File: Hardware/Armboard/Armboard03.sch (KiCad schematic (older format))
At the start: 8 parts

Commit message: H-Bridge completed
Completed the H-Bridge Hierarchal Sheet
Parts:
- U? (x8): symbol MRDT_Shields:TM4C129E_Launchpad -> Armboard-rescue:TM4C129E_Launchpad-MRDT_Shields
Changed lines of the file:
@@
 $EndDescr
 $Comp
-L MRDT_Shields:TM4C129E_Launchpad U?
+L Armboard-rescue:TM4C129E_Launchpad-MRDT_Shields U?
 U 1 1 5F752485
 P 3810 3400
@@
 $EndComp
 $Comp
-L MRDT_Shields:TM4C129E_Launchpad U?
+L Armboard-rescue:TM4C129E_Launchpad-MRDT_Shields U?
 U 2 1 5F752EEB
 P 4310 3400
@@
 $EndComp
 $Comp
-L MRDT_Shields:TM4C129E_Launchpad U?
+L Armboard-rescue:TM4C129E_Launchpad-MRDT_Shields U?
 U 3 1 5F753E3C
 P 3800 5520
@@
 $EndComp
 $Comp
-L MRDT_Shields:TM4C129E_Launchpad U?
+L Armboard-rescue:TM4C129E_Launchpad-MRDT_Shields U?
 U 4 1 5F754D60
 P 4300 5520
@@
 $EndComp
 $Comp
-L MRDT_Shields:TM4C129E_Launchpad U?
+L Armboard-rescue:TM4C129E_Launchpad-MRDT_Shields U?
 U 5 1 5F755C93
 P 6400 3390
@@
 $EndComp
 $Comp
-L MRDT_Shields:TM4C129E_Launchpad U?
+L Armboard-rescue:TM4C129E_Launchpad-MRDT_Shields U?
 U 6 1 5F7570A2
 P 6900 3390
@@
 $EndComp
 $Comp
-L MRDT_Shields:TM4C129E_Launchpad U?
+L Armboard-rescue:TM4C129E_Launchpad-MRDT_Shields U?
 U 7 1 5F757FE4
 P 6420 5520
@@
 $EndComp
 $Comp
-L MRDT_Shields:TM4C129E_Launchpad U?
+L Armboard-rescue:TM4C129E_Launchpad-MRDT_Shields U?
 U 8 1 5F7598C0
 P 6920 5520

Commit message: Added serial pins, limit switches, titles, and indicators
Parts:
- U? (x8): symbol Armboard-rescue:TM4C129E_Launchpad-MRDT_Shields -> Armboard-rescue:TM4C129E_Launchpad-MRDT_Shields-Armboard-rescue
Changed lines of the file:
@@
 $EndDescr
 $Comp
-L Armboard-rescue:TM4C129E_Launchpad-MRDT_Shields U?
+L Armboard-rescue:TM4C129E_Launchpad-MRDT_Shields-Armboard-rescue U?
 U 1 1 5F752485
 P 3810 3400
@@
 $EndComp
 $Comp
-L Armboard-rescue:TM4C129E_Launchpad-MRDT_Shields U?
+L Armboard-rescue:TM4C129E_Launchpad-MRDT_Shields-Armboard-rescue U?
 U 2 1 5F752EEB
 P 4310 3400
@@
 $EndComp
 $Comp
-L Armboard-rescue:TM4C129E_Launchpad-MRDT_Shields U?
+L Armboard-rescue:TM4C129E_Launchpad-MRDT_Shields-Armboard-rescue U?
 U 3 1 5F753E3C
 P 3800 5520
@@
 $EndComp
 $Comp
-L Armboard-rescue:TM4C129E_Launchpad-MRDT_Shields U?
+L Armboard-rescue:TM4C129E_Launchpad-MRDT_Shields-Armboard-rescue U?
 U 4 1 5F754D60
 P 4300 5520
@@
 $EndComp
 $Comp
-L Armboard-rescue:TM4C129E_Launchpad-MRDT_Shields U?
+L Armboard-rescue:TM4C129E_Launchpad-MRDT_Shields-Armboard-rescue U?
 U 5 1 5F755C93
 P 6400 3390
@@
 $EndComp
 $Comp
-L Armboard-rescue:TM4C129E_Launchpad-MRDT_Shields U?
+L Armboard-rescue:TM4C129E_Launchpad-MRDT_Shields-Armboard-rescue U?
 U 6 1 5F7570A2
 P 6900 3390
@@
 $EndComp
 $Comp
-L Armboard-rescue:TM4C129E_Launchpad-MRDT_Shields U?
+L Armboard-rescue:TM4C129E_Launchpad-MRDT_Shields-Armboard-rescue U?
 U 7 1 5F757FE4
 P 6420 5520
@@
 $EndComp
 $Comp
-L Armboard-rescue:TM4C129E_Launchpad-MRDT_Shields U?
+L Armboard-rescue:TM4C129E_Launchpad-MRDT_Shields-Armboard-rescue U?
 U 8 1 5F7598C0
 P 6920 5520

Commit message: Tiva Updates
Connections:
- net +3V3: now reaches U?.+3V3 (A1_1)
- net +3V3: now also U?.+3V3' (A2_1)
- net LS_3: now reaches U?.PB2 (A1_9)
- net LS_4: now reaches U?.PB3 (A1_10)
- net Rx_1_Tiva: now reaches U?.PC4 (A1_3)
- net Tx_1_Tiva: now reaches U?.PC5 (A1_4)
- net GND: now reaches U?.GND (B1_2)
- net GND: now also U?.GND (B2_2), U?.GND (D1_1), U?.GND (D2_1)
- net Enc_1_PWM: now reaches U?.PF1 (C1_1)
- net Enc_2_PWM: now reaches U?.PF2 (C1_2)
- net Enc_3_PWM: now reaches U?.PF3 (C1_3)
- net Enc_4_PWM: now reaches U?.PG0 (C1_4)
- net Rx_3_Tiva: now reaches U?.PP0 (A2_3)
- net Tx_3_Tiva: now reaches U?.PP1 (A2_4)
- net LS_1: now reaches U?.PA4 (B2_9)
- net LS_2: now reaches U?.PA5 (B2_10)
- net Rx_2_Tiva: now reaches U?.PK0 (B2_5)
- net Tx_2_Tiva: now reaches U?.PK1 (B2_6)
- net Enc_5_PWM: now reaches U?.PG1 (C2_1)
- net Laser_Control: now reaches U?.PH0 (C2_7)
- net Solenoid_Actuation: now reaches U?.PH1 (C2_8)
- net Enc_6_PWM: now reaches U?.PK4 (C2_2)
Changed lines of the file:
@@
 	-1   0    0    -1
 $EndComp
+$Comp
+L power:GND #PWR?
+U 1 1 5F83BEC8
+P 4800 2600
+F 0 "#PWR?" H 4800 2350 50  0001 C CNN
+F 1 "GND" H 4805 2427 50  0000 C CNN
+F 2 "" H 4800 2600 50  0001 C CNN
+F 3 "" H 4800 2600 50  0001 C CNN
+	1    4800 2600
+	1    0    0    -1
+$EndComp
+Wire Wire Line
+	4500 2550 4510 2550
+Wire Wire Line
+	4800 2550 4800 2600
+Connection ~ 4510 2550
+Wire Wire Line
+	4510 2550 4800 2550
+$Comp
+L power:+3.3V #PWR?
+U 1 1 5F83D247
+P 3400 2450
+F 0 "#PWR?" H 3400 2300 50  0001 C CNN
+F 1 "+3.3V" V 3415 2578 50  0000 L CNN
+F 2 "" H 3400 2450 50  0001 C CNN
+F 3 "" H 3400 2450 50  0001 C CNN
+	1    3400 2450
+	0    -1   -1   0
+$EndComp
+Wire Wire Line
+	3400 2450 3610 2450
+$Comp
+L power:+3.3V #PWR?
+U 1 1 5F83FA68
+P 5990 2440
+F 0 "#PWR?" H 5990 2290 50  0001 C CNN
+F 1 "+3.3V" V 6005 2568 50  0000 L CNN
+F 2 "" H 5990 2440 50  0001 C CNN
+F 3 "" H 5990 2440 50  0001 C CNN
+	1    5990 2440
+	0    -1   -1   0
+$EndComp
+Wire Wire Line
+	5990 2440 6200 2440
+$Comp
+L power:GND #PWR?
+U 1 1 5F83FD93
+P 7390 2560
+F 0 "#PWR?" H 7390 2310 50  0001 C CNN
+F 1 "GND" H 7395 2387 50  0000 C CNN
+F 2 "" H 7390 2560 50  0001 C CNN
+F 3 "" H 7390 2560 50  0001 C CNN
+	1    7390 2560
+	1    0    0    -1
+$EndComp
+$Comp
+L power:GND #PWR?
+U 1 1 5F83FFBB
+P 4790 4620
+F 0 "#PWR?" H 4790 4370 50  0001 C CNN
+F 1 "GND" H 4795 4447 50  0000 C CNN
+F 2 "" H 4790 4620 50  0001 C CNN
+F 3 "" H 4790 4620 50  0001 C CNN
+	1    4790 4620
+	1    0    0    -1
+$EndComp
+Wire Wire Line
+	4790 4570 4790 4620
+Wire Wire Line
+	4500 4570 4790 4570
+$Comp
+L power:GND #PWR?
+U 1 1 5F8401EF
+P 7410 4620
+F 0 "#PWR?" H 7410 4370 50  0001 C CNN
+F 1 "GND" H 7415 4447 50  0000 C CNN
+F 2 "" H 7410 4620 50  0001 C CNN
+F 3 "" H 7410 4620 50  0001 C CNN
+	1    7410 4620
+	1    0    0    -1
+$EndComp
+Wire Wire Line
+	7410 4570 7410 4620
+Wire Wire Line
+	7120 4570 7410 4570
+Text GLabel 3530 4570 0    50   Input ~ 0
+Enc_1_PWM
+Wire Wire Line
+	3600 4570 3530 4570
+Text GLabel 3530 4670 0    50   Input ~ 0
+Enc_2_PWM
+Wire Wire Line
+	3600 4670 3530 4670
+Text GLabel 3530 4770 0    50   Input ~ 0
+Enc_3_PWM
+Wire Wire Line
+	3600 4770 3530 4770
+Text GLabel 3530 4870 0    50   Input ~ 0
+Enc_4_PWM
+Wire Wire Line
+	3600 4870 3530 4870
+Text GLabel 6150 4570 0    50   Input ~ 0
+Enc_5_PWM
+Wire Wire Line
+	6220 4570 6150 4570
+Text GLabel 6150 4670 0    50   Input ~ 0
+Enc_6_PWM
+Wire Wire Line
+	6220 4670 6150 4670
+Text GLabel 7170 3340 2    50   Input ~ 0
+LS_2
+Wire Wire Line
+	7100 3340 7170 3340
+Text GLabel 7170 3240 2    50   Input ~ 0
+LS_1
+Wire Wire Line
+	7100 3240 7170 3240
+Text GLabel 3540 3250 0    50   Input ~ 0
+LS_3
+Wire Wire Line
+	3610 3250 3540 3250
+Text GLabel 3540 3350 0    50   Input ~ 0
+LS_4
+Wire Wire Line
+	3610 3350 3540 3350
+Text GLabel 6150 5170 0    50   Input ~ 0
+Laser_Control
+Wire Wire Line
+	6220 5170 6150 5170
+Text GLabel 6150 5270 0    50   Input ~ 0
+Solenoid_Actuation
+Wire Wire Line
+	6220 5270 6150 5270
+Text GLabel 3540 2650 0    50   Input ~ 0
+Rx_1_Tiva
+Wire Wire Line
+	3610 2650 3540 2650
+Text GLabel 3540 2750 0    50   Input ~ 0
+Tx_1_Tiva
+Wire Wire Line
+	3610 2750 3540 2750
+Text GLabel 7170 2940 2    50   Input ~ 0
+Tx_2_Tiva
+Wire Wire Line
+	7100 2940 7170 2940
+Text GLabel 7170 2840 2    50   Input ~ 0
+Rx_2_Tiva
+Wire Wire Line
+	7100 2840 7170 2840
+Wire Wire Line
+	7100 2540 7390 2540
+Wire Wire Line
+	7390 2540 7390 2560
+Text GLabel 6130 2640 0    50   Input ~ 0
+Rx_3_Tiva
+Wire Wire Line
+	6200 2640 6130 2640
+Text GLabel 6130 2740 0    50   Input ~ 0
+Tx_3_Tiva
+Wire Wire Line
+	6200 2740 6130 2740
 $EndSCHEMATC

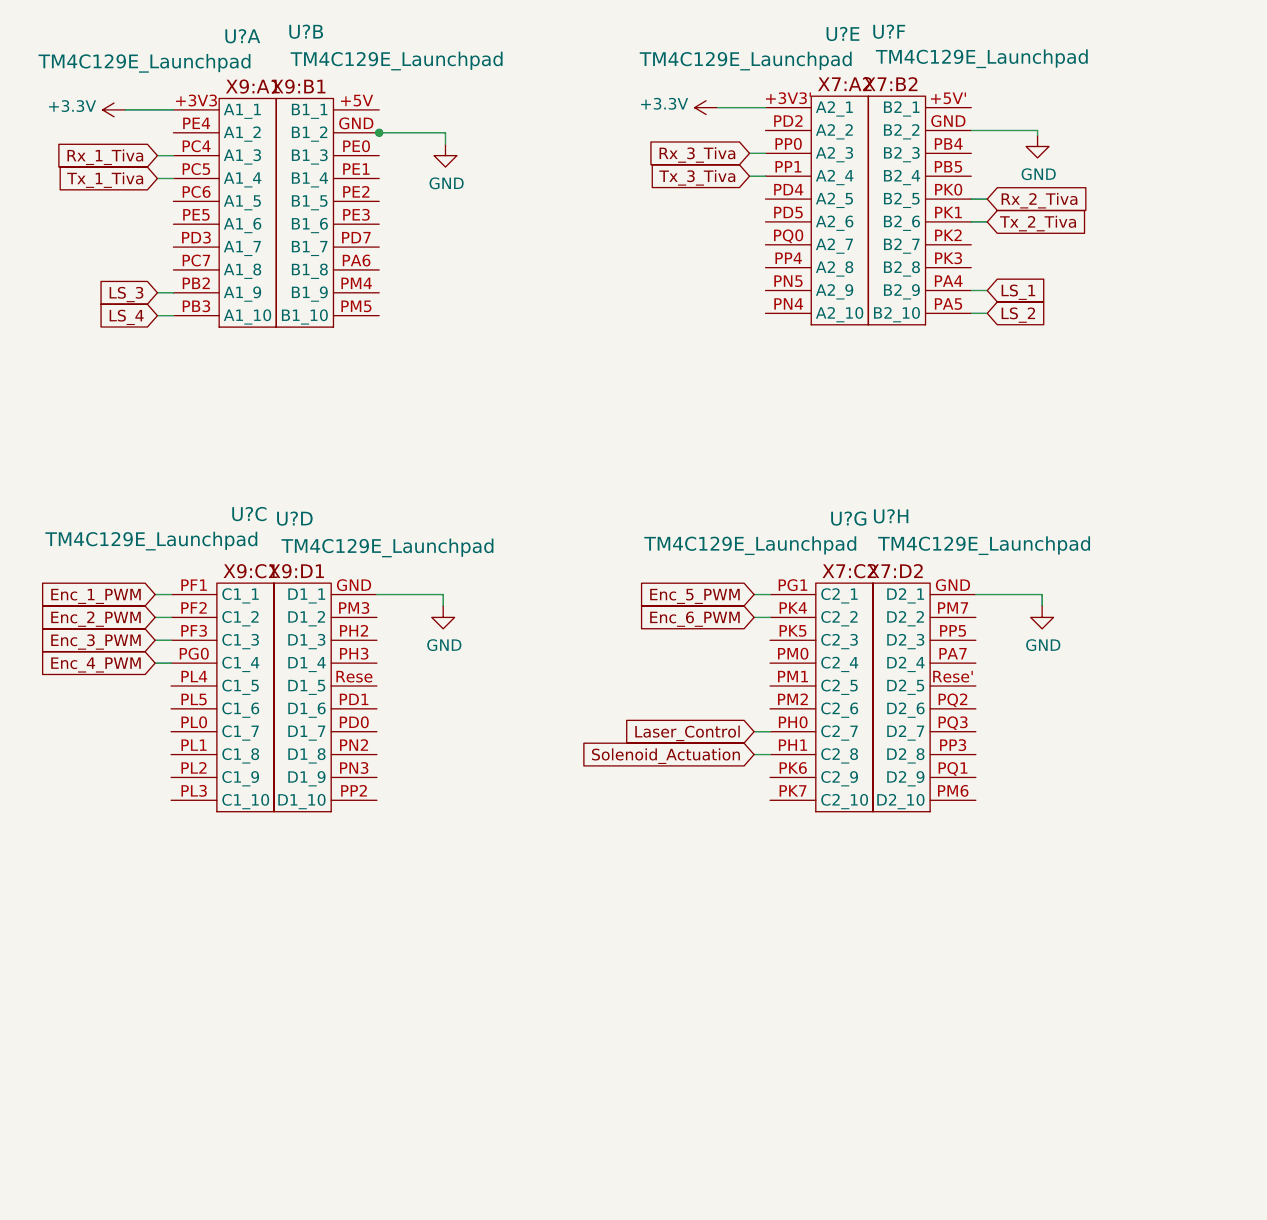
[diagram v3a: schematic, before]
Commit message: Formatted GNDs and added motor toggle buttons
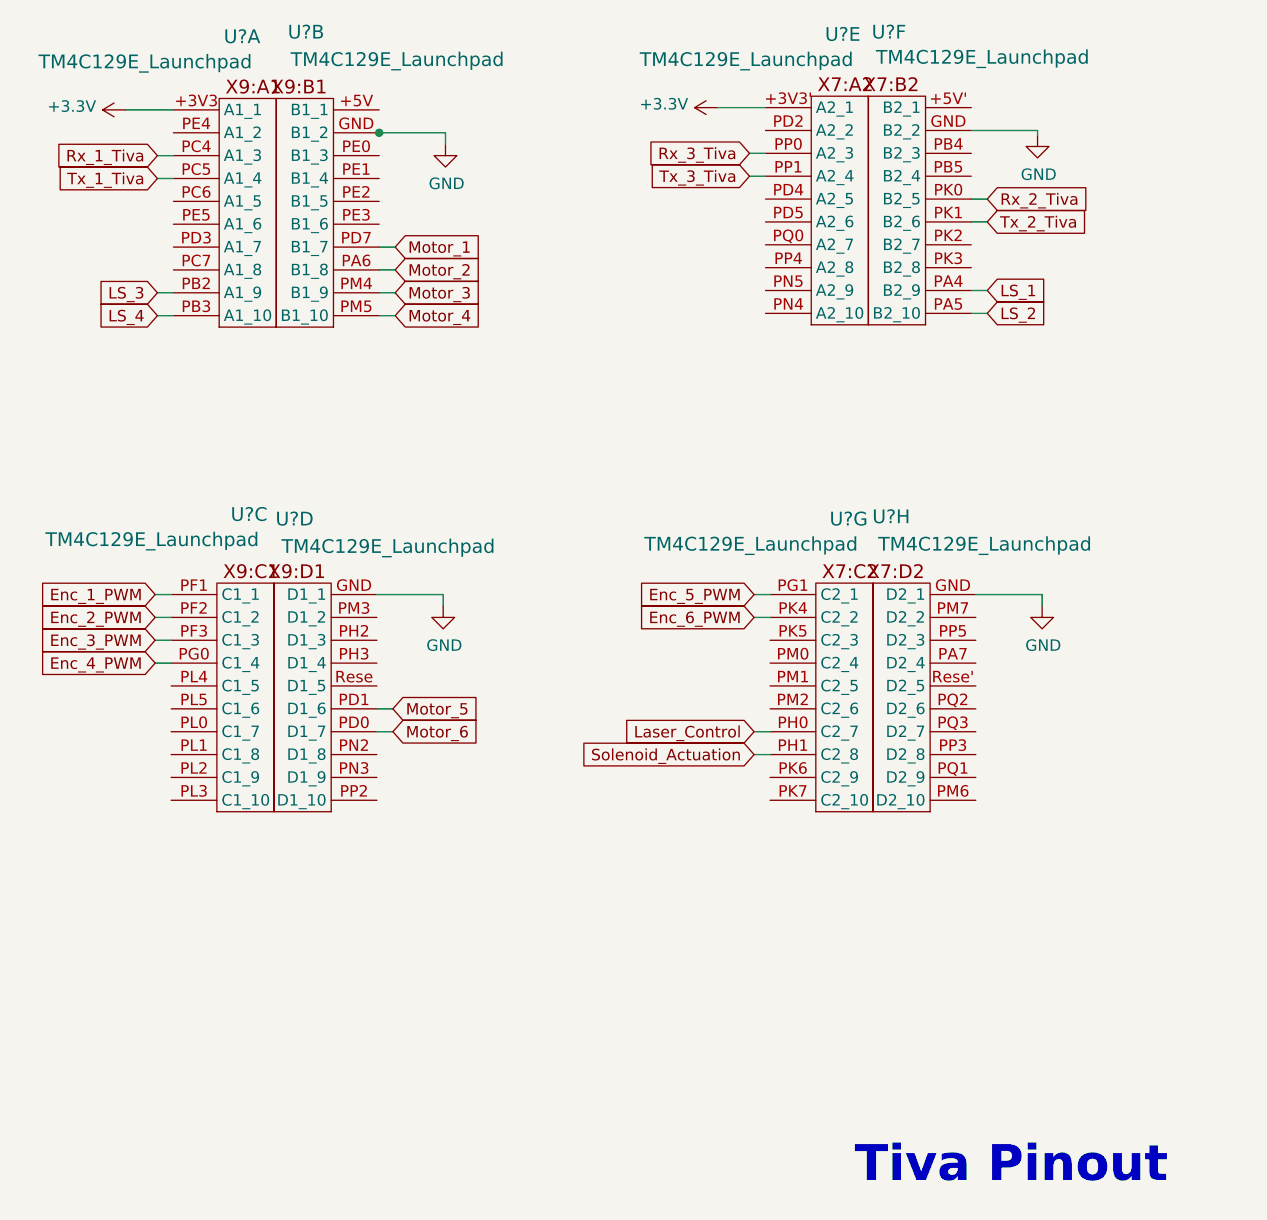
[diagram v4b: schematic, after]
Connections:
- net Motor_2: now reaches U?.PA6 (B1_8)
- net Motor_1: now reaches U?.PD7 (B1_7)
- net Motor_3: now reaches U?.PM4 (B1_9)
- net Motor_4: now reaches U?.PM5 (B1_10)
- net Motor_6: now reaches U?.PD0 (D1_7)
- net Motor_5: now reaches U?.PD1 (D1_6)
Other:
- note added: "Tiva Pinout"
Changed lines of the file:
@@
 Wire Wire Line
 	6200 2740 6130 2740
+Text GLabel 4580 3150 2    50   Input ~ 0
+Motor_2
+Wire Wire Line
+	4510 3150 4580 3150
+Text GLabel 4580 3050 2    50   Input ~ 0
+Motor_1
+Wire Wire Line
+	4510 3050 4580 3050
+Text GLabel 4580 3350 2    50   Input ~ 0
+Motor_4
+Wire Wire Line
+	4510 3350 4580 3350
+Text GLabel 4580 3250 2    50   Input ~ 0
+Motor_3
+Wire Wire Line
+	4510 3250 4580 3250
+Text GLabel 4570 5170 2    50   Input ~ 0
+Motor_6
+Wire Wire Line
+	4500 5170 4570 5170
+Text GLabel 4570 5070 2    50   Input ~ 0
+Motor_5
+Wire Wire Line
+	4500 5070 4570 5070
+Text Notes 6590 7160 0    157  ~ 31
+Tiva Pinout
 $EndSCHEMATC

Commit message: Fixed buttons/switches page, changed resistor values, fixed some tiva connections
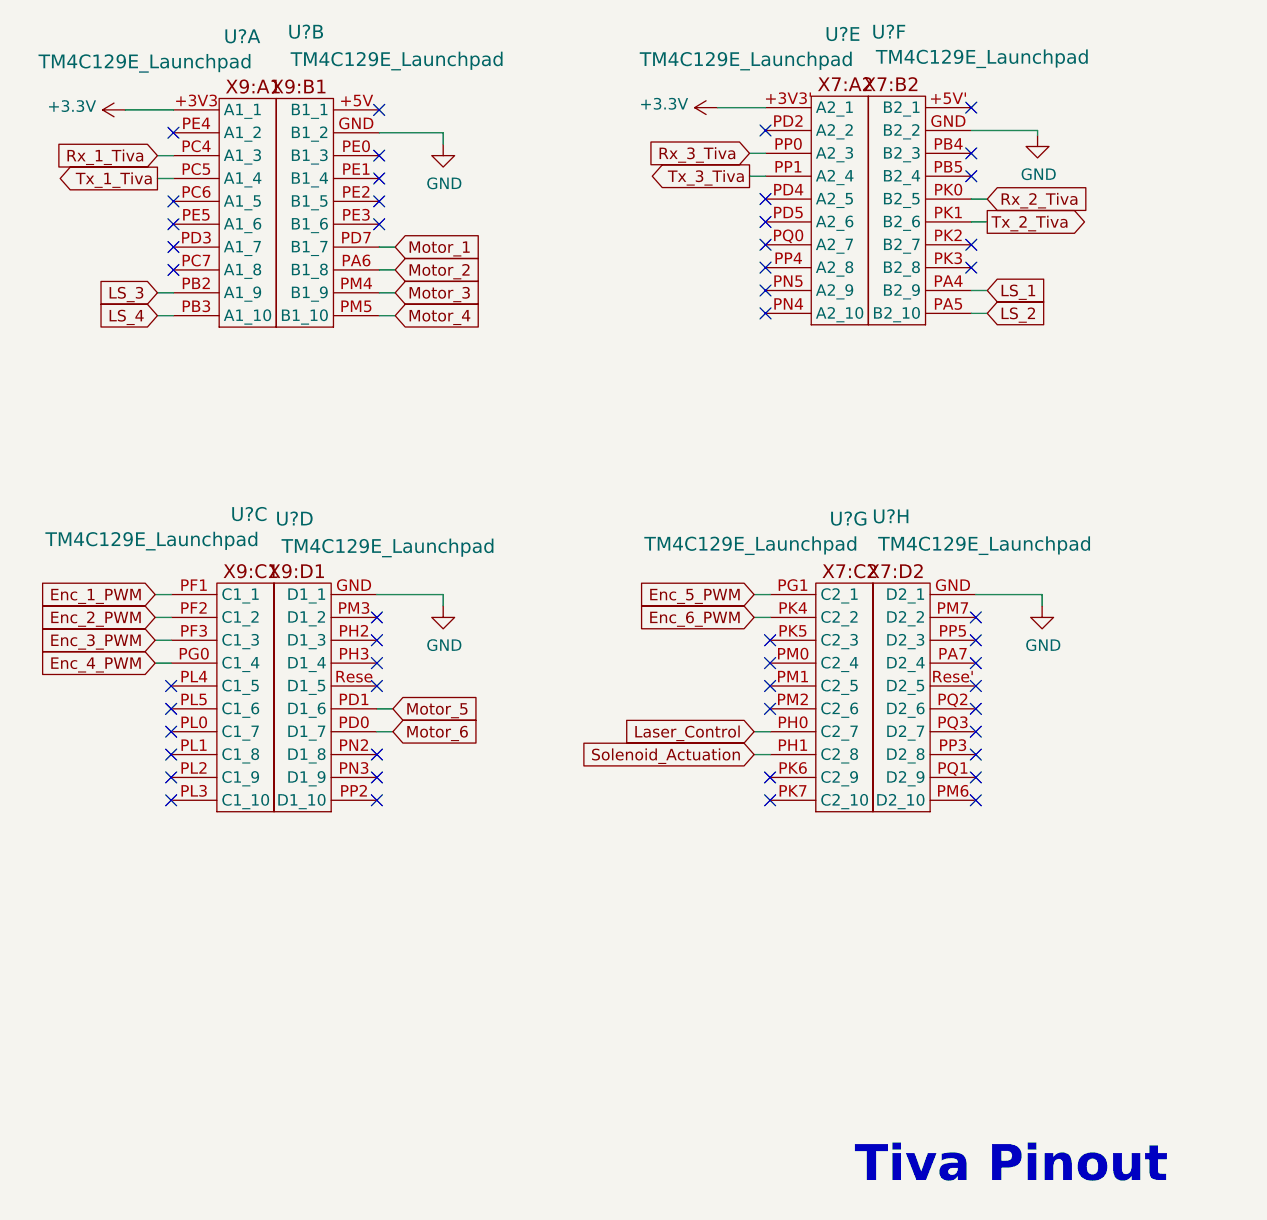
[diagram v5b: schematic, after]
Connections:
- no-connect marks 0 -> 50
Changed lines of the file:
@@
 L power:GND #PWR?
 U 1 1 5F83BEC8
-P 4800 2600
-F 0 "#PWR?" H 4800 2350 50  0001 C CNN
-F 1 "GND" H 4805 2427 50  0000 C CNN
-F 2 "" H 4800 2600 50  0001 C CNN
-F 3 "" H 4800 2600 50  0001 C CNN
-	1    4800 2600
-	1    0    0    -1
-$EndComp
-Wire Wire Line
-	4500 2550 4510 2550
-Wire Wire Line
-	4800 2550 4800 2600
-Connection ~ 4510 2550
-Wire Wire Line
-	4510 2550 4800 2550
+P 4790 2600
+F 0 "#PWR?" H 4790 2350 50  0001 C CNN
+F 1 "GND" H 4795 2427 50  0000 C CNN
+F 2 "" H 4790 2600 50  0001 C CNN
+F 3 "" H 4790 2600 50  0001 C CNN
+	1    4790 2600
+	1    0    0    -1
+$EndComp
+Wire Wire Line
+	4790 2550 4790 2600
 $Comp
 L power:+3.3V #PWR?
@@
 Wire Wire Line
 	3610 2650 3540 2650
-Text GLabel 3540 2750 0    50   Input ~ 0
+Text GLabel 3540 2750 0    50   Output ~ 0
 Tx_1_Tiva
 Wire Wire Line
 	3610 2750 3540 2750
-Text GLabel 7170 2940 2    50   Input ~ 0
+Text GLabel 7170 2940 2    50   Output ~ 0
 Tx_2_Tiva
 Wire Wire Line
@@
 Wire Wire Line
 	6200 2640 6130 2640
-Text GLabel 6130 2740 0    50   Input ~ 0
+Text GLabel 6130 2740 0    50   Output ~ 0
 Tx_3_Tiva
 Wire Wire Line
@@
 Text Notes 6590 7160 0    157  ~ 31
 Tiva Pinout
+Wire Wire Line
+	4510 2550 4790 2550
+NoConn ~ 3610 2550
+NoConn ~ 3610 2850
+NoConn ~ 3610 2950
+NoConn ~ 3610 3050
+NoConn ~ 3610 3150
+NoConn ~ 4510 2650
+NoConn ~ 4510 2750
+NoConn ~ 4510 2850
+NoConn ~ 4510 2950
+NoConn ~ 4510 2450
+NoConn ~ 6200 2540
+NoConn ~ 6200 2840
+NoConn ~ 6200 2940
+NoConn ~ 6200 3040
+NoConn ~ 6200 3140
+NoConn ~ 6200 3240
+NoConn ~ 6200 3340
+NoConn ~ 7100 2440
+NoConn ~ 7100 2640
+NoConn ~ 7100 2740
+NoConn ~ 7100 3040
+NoConn ~ 7100 3140
+NoConn ~ 3600 4970
+NoConn ~ 3600 5070
+NoConn ~ 3600 5170
+NoConn ~ 3600 5270
+NoConn ~ 3600 5370
+NoConn ~ 3600 5470
+NoConn ~ 4500 4670
+NoConn ~ 4500 4770
+NoConn ~ 4500 4870
+NoConn ~ 4500 4970
+NoConn ~ 4500 5270
+NoConn ~ 4500 5370
+NoConn ~ 4500 5470
+NoConn ~ 6220 4770
+NoConn ~ 6220 4870
+NoConn ~ 6220 4970
+NoConn ~ 6220 5070
+NoConn ~ 6220 5370
+NoConn ~ 6220 5470
+NoConn ~ 7120 4670
+NoConn ~ 7120 4770
+NoConn ~ 7120 4870
+NoConn ~ 7120 4970
+NoConn ~ 7120 5070
+NoConn ~ 7120 5170
+NoConn ~ 7120 5270
+NoConn ~ 7120 5370
+NoConn ~ 7120 5470
 $EndSCHEMATC
